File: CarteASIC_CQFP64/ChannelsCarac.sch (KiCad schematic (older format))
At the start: 29 parts, among them U1 ASIC_JUICE

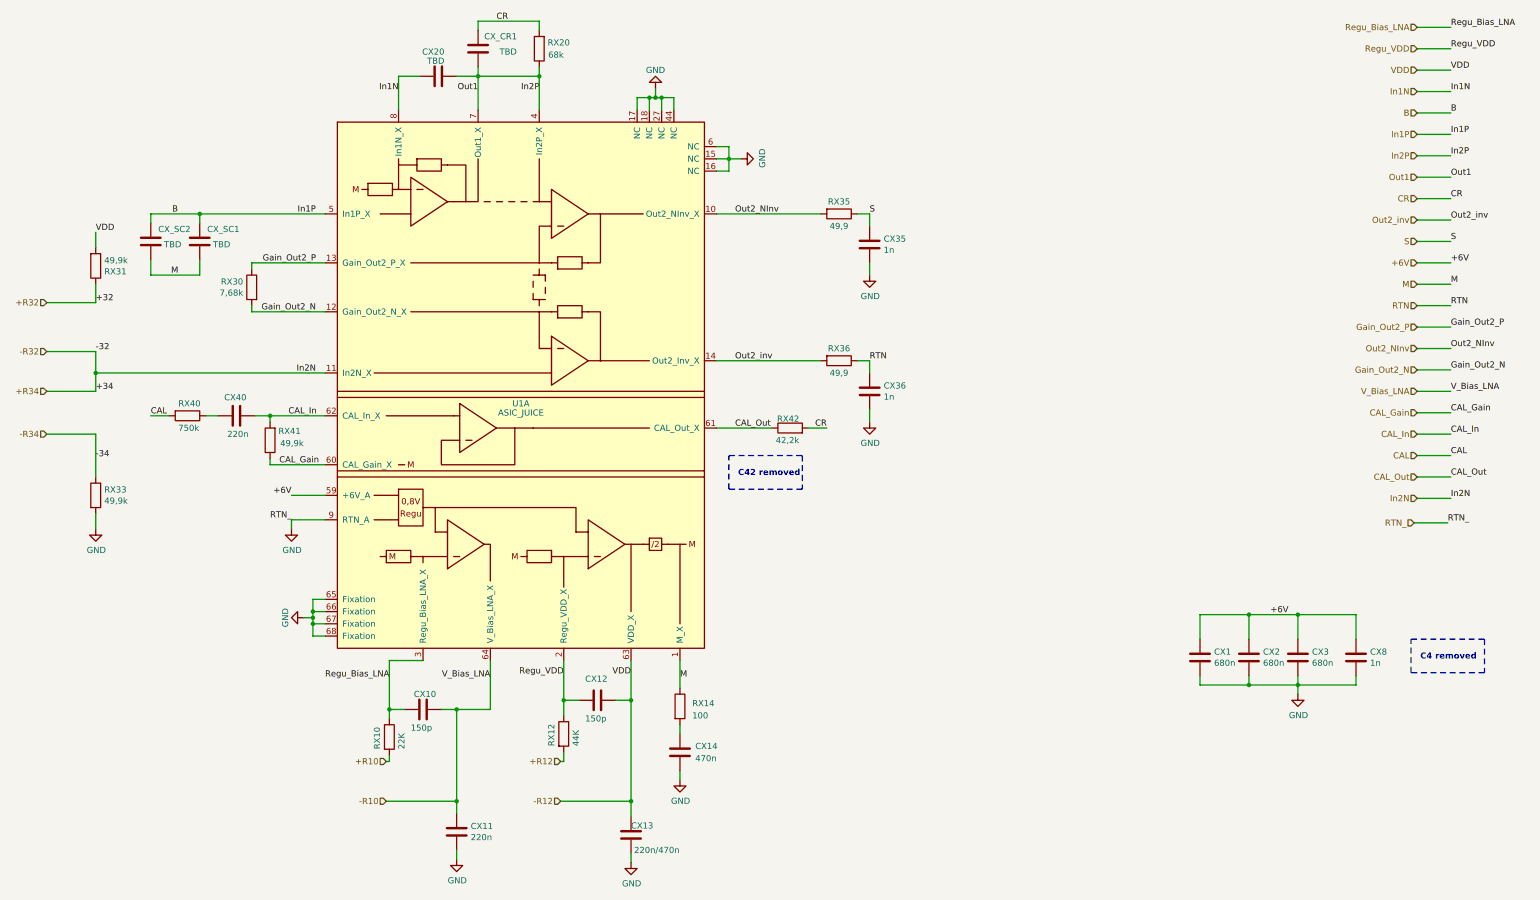
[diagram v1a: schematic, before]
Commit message: Mise en conformité valeurs PFM
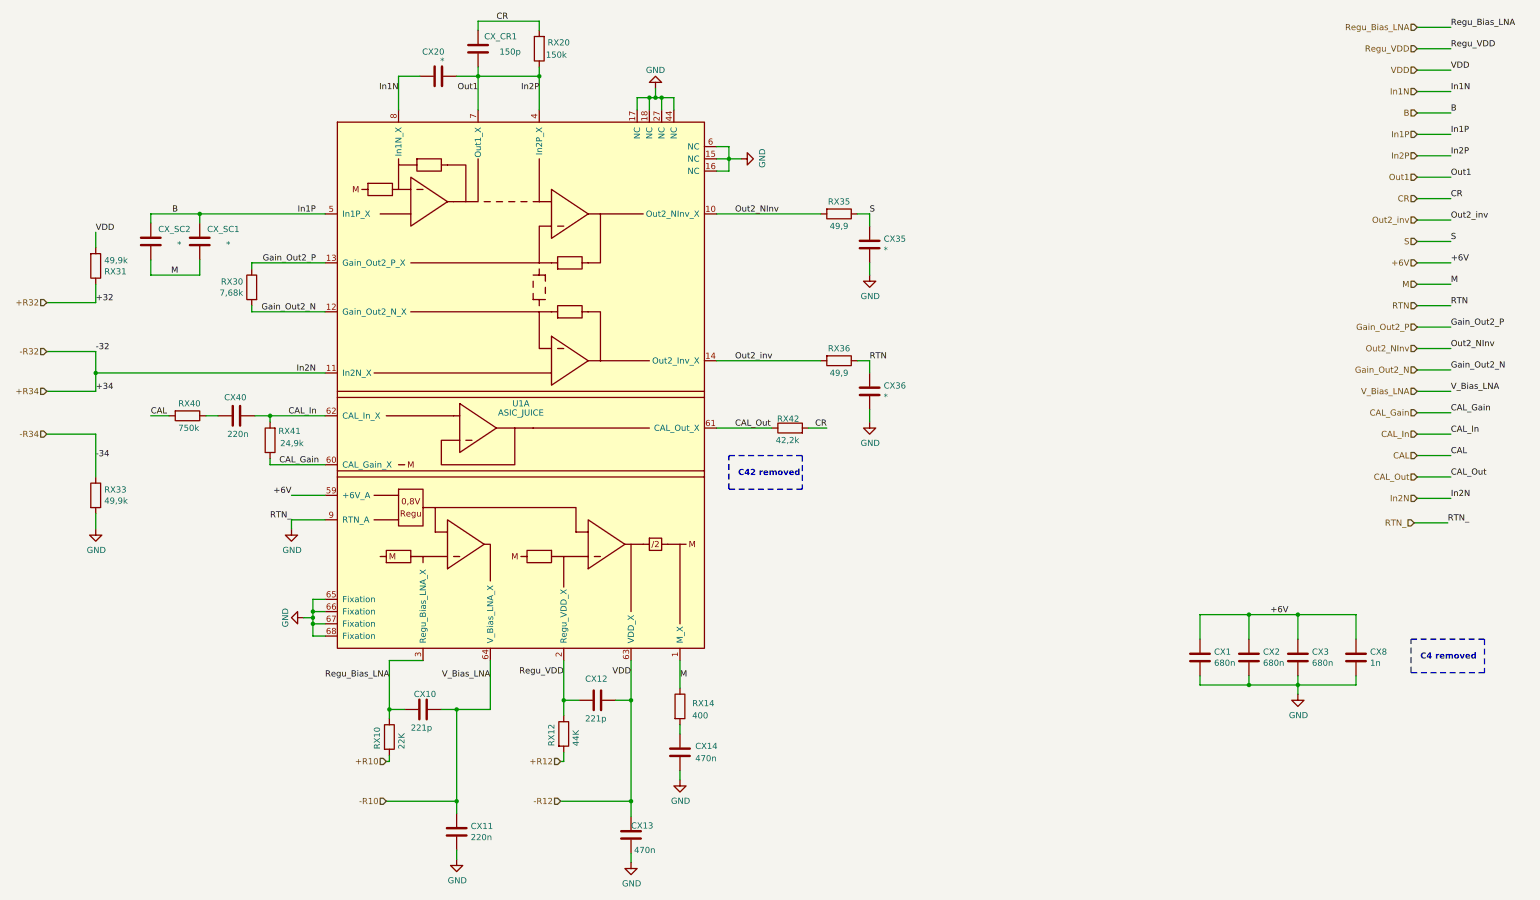
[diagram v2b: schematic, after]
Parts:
- CX10, CX12: value 150p -> 221p
- CX13: value 220n/470n -> 470n
- CX20, CX_SC1, CX_SC2: value TBD -> *
- CX35, CX36: value 1n -> *
- CX_CR1: value TBD -> 150p
- RX14: value 100 -> 400
- RX20: value 68k -> 150k
- RX41: value 49,9k -> 24,9k
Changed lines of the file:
@@
 AR Path="/5D9D35E7/5D83A418/5D7F2F74" Ref="CY12"  Part="1"
 F 0 "CX12" V 8075 7300 50  0000 L CNN
-F 1 "150p" V 8400 7300 50  0000 L CNN
+F 1 "221p" V 8400 7300 50  0000 L CNN
 F 2 "Capacitor_SMD:C_0603_1608Metric_Pad1.05x0.95mm_HandSolder" H 8288 7250 50  0001 C CNN
 F 3 "~" H 8250 7400 50  0001 C CNN
@@
 AR Path="/5D9D35E7/5D843251/5D8E789D" Ref="#PWR?"  Part="1"
 AR Path="/5D9D35E7/5D83A418/5D8E789D" Ref="#PWR?"  Part="1"
-F 0 "#PWR0117" H 8925 7800 50  0001 C CNN
+F 0 "#PWR0106" H 8925 7800 50  0001 C CNN
 F 1 "GND" H 8930 7877 50  0000 C CNN
 F 2 "" H 8925 8050 50  0001 C CNN
@@
 AR Path="/5D9D35E7/5D843251/5D8E7505" Ref="#PWR?"  Part="1"
 AR Path="/5D9D35E7/5D83A418/5D8E7505" Ref="#PWR?"  Part="1"
-F 0 "#PWR0118" H 8525 8475 50  0001 C CNN
+F 0 "#PWR0107" H 8525 8475 50  0001 C CNN
 F 1 "GND" H 8530 8552 50  0000 C CNN
 F 2 "" H 8525 8725 50  0001 C CNN
@@
 AR Path="/5D9D35E7/5D83A418/5D7F3986" Ref="CY35"  Part="1"
 F 0 "CX35" H 10590 3721 50  0000 L CNN
-F 1 "1n" H 10590 3630 50  0000 L CNN
+F 1 "*" H 10590 3630 50  0000 L CNN
 F 2 "Capacitor_SMD:C_0603_1608Metric_Pad1.05x0.95mm_HandSolder" H 10513 3525 50  0001 C CNN
 F 3 "~" H 10475 3675 50  0001 C CNN
@@
 AR Path="/5D9D35E7/5D83A418/5D7F398C" Ref="CY36"  Part="1"
 F 0 "CX36" H 10590 4921 50  0000 L CNN
-F 1 "1n" H 10590 4830 50  0000 L CNN
+F 1 "*" H 10590 4830 50  0000 L CNN
 F 2 "Capacitor_SMD:C_0603_1608Metric_Pad1.05x0.95mm_HandSolder" H 10513 4725 50  0001 C CNN
 F 3 "~" H 10475 4875 50  0001 C CNN
@@
 AR Path="/5D9D35E7/5D843251/5D96B6E7" Ref="#PWR?"  Part="1"
 AR Path="/5D9D35E7/5D83A418/5D96B6E7" Ref="#PWR?"  Part="1"
-F 0 "#PWR0119" H 10475 3675 50  0001 C CNN
+F 0 "#PWR0108" H 10475 3675 50  0001 C CNN
 F 1 "GND" H 10480 3752 50  0000 C CNN
 F 2 "" H 10475 3925 50  0001 C CNN
@@
 AR Path="/5D9D35E7/5D843251/5D96BF67" Ref="#PWR?"  Part="1"
 AR Path="/5D9D35E7/5D83A418/5D96BF67" Ref="#PWR?"  Part="1"
-F 0 "#PWR0120" H 10475 4875 50  0001 C CNN
+F 0 "#PWR0109" H 10475 4875 50  0001 C CNN
 F 1 "GND" H 10480 4952 50  0000 C CNN
 F 2 "" H 10475 5125 50  0001 C CNN
@@
 AR Path="/5D9D35E7/5D83A418/5D838645" Ref="RY20"  Part="1"
 F 0 "RX20" H 7525 2025 50  0000 L CNN
-F 1 "68k" H 7575 2125 50  0000 L CNN
+F 1 "150k" H 7550 2125 50  0000 L CNN
 F 2 "Resistor_SMD:R_0805_2012Metric_Pad1.15x1.40mm_HandSolder" V 7705 2075 50  0001 C CNN
 F 3 "~" H 7775 2075 50  0001 C CNN
@@
 AR Path="/5D9D35E7/5D843251/5D884FFA" Ref="#PWR?"  Part="1"
 AR Path="/5D9D35E7/5D83A418/5D884FFA" Ref="#PWR?"  Part="1"
-F 0 "#PWR0123" H 13975 7100 50  0001 C CNN
+F 0 "#PWR0112" H 13975 7100 50  0001 C CNN
 F 1 "GND" H 13980 7177 50  0000 C CNN
 F 2 "" H 13975 7350 50  0001 C CNN
@@
 AR Path="/5D9D35E7/5D843251/5E598485" Ref="#PWR?"  Part="1"
 AR Path="/5D9D35E7/5D83A418/5E598485" Ref="#PWR?"  Part="1"
-F 0 "#PWR0124" H 5850 6475 50  0001 C CNN
+F 0 "#PWR0113" H 5850 6475 50  0001 C CNN
 F 1 "GND" H 5850 6575 50  0000 C CNN
 F 2 "" H 5850 6725 50  0001 C CNN
@@
 AR Path="/5D9D35E7/5D843251/5E59CF62" Ref="#PWR?"  Part="1"
 AR Path="/5D9D35E7/5D83A418/5E59CF62" Ref="#PWR?"  Part="1"
-F 0 "#PWR0125" H 5750 5750 50  0001 C CNN
+F 0 "#PWR0114" H 5750 5750 50  0001 C CNN
 F 1 "GND" H 5755 5827 50  0000 C CNN
 F 2 "" H 5750 6000 50  0001 C CNN
@@
 AR Path="/5D9D35E7/5D843251/5E5A15CF" Ref="#PWR?"  Part="1"
 AR Path="/5D9D35E7/5D83A418/5E5A15CF" Ref="#PWR?"  Part="1"
-F 0 "#PWR0126" H 9425 2725 50  0001 C CNN
+F 0 "#PWR0115" H 9425 2725 50  0001 C CNN
 F 1 "GND" H 9430 2802 50  0000 C CNN
 F 2 "" H 9425 2975 50  0001 C CNN
@@
 AR Path="/5D9D35E7/5D843251/5E7A4666" Ref="#PWR?"  Part="1"
 AR Path="/5D9D35E7/5D83A418/5E7A4666" Ref="#PWR?"  Part="1"
-F 0 "#PWR0127" H 8725 2150 50  0001 C CNN
+F 0 "#PWR0116" H 8725 2150 50  0001 C CNN
 F 1 "GND" H 8725 2250 50  0000 C CNN
 F 2 "" H 8725 2400 50  0001 C CNN
@@
 AR Path="/5D9D35E7/5D83A418/5D917477" Ref="CY20"  Part="1"
 F 0 "CX20" V 7150 2250 50  0000 L CNN
-F 1 "TBD" V 7075 2250 50  0000 L CNN
+F 1 "*" V 7075 2250 50  0000 L CNN
 F 2 "Capacitor_SMD:C_0603_1608Metric_Pad1.05x0.95mm_HandSolder" H 6988 2150 50  0001 C CNN
 F 3 "~" H 6950 2300 50  0001 C CNN
@@
 AR Path="/5D9D35E7/5D83A418/5D92ED61" Ref="CY_CR"  Part="1"
 F 0 "CX_CR1" H 7325 2175 50  0000 L CNN
-F 1 "TBD" H 7450 2050 50  0000 L CNN
+F 1 "150p" H 7450 2050 50  0000 L CNN
 F 2 "Capacitor_SMD:C_0603_1608Metric_Pad1.05x0.95mm_HandSolder" H 7313 1925 50  0001 C CNN
 F 3 "~" H 7275 2075 50  0001 C CNN
@@
 AR Path="/5D9D35E7/5D83A418/5D987FFC" Ref="CY_SC1"  Part="1"
 F 0 "CX_SC1" H 4675 3750 50  0000 L CNN
-F 1 "TBD" H 4750 3625 50  0000 L CNN
+F 1 "*" H 4750 3625 50  0000 L CNN
 F 2 "Capacitor_SMD:C_0603_1608Metric_Pad1.05x0.95mm_HandSolder" H 5038 3500 50  0001 C CNN
 F 3 "~" H 5000 3650 50  0001 C CNN
@@
 AR Path="/5D9D35E7/5D83A418/5D9886E7" Ref="CY_SC2"  Part="1"
 F 0 "CX_SC2" H 4275 3750 50  0000 L CNN
-F 1 "TBD" H 4350 3625 50  0000 L CNN
+F 1 "*" H 4350 3625 50  0000 L CNN
 F 2 "Capacitor_SMD:C_0603_1608Metric_Pad1.05x0.95mm_HandSolder" H 4638 3500 50  0001 C CNN
 F 3 "~" H 4600 3650 50  0001 C CNN
@@
 AR Path="/5D9D35E7/5D843251/5D8A9AA9" Ref="#PWR?"  Part="1"
 AR Path="/5D9D35E7/5D83A418/5D8A9AA9" Ref="#PWR?"  Part="1"
-F 0 "#PWR0121" H 7100 8450 50  0001 C CNN
+F 0 "#PWR0110" H 7100 8450 50  0001 C CNN
 F 1 "GND" H 7105 8527 50  0000 C CNN
 F 2 "" H 7100 8700 50  0001 C CNN
@@
 AR Path="/5D9D35E7/5D83A418/5D7F2F7A" Ref="CY13"  Part="1"
 F 0 "CX13" H 8525 8575 50  0000 L CNN
-F 1 "220n/470n" H 8550 8375 50  0000 L CNN
+F 1 "470n" H 8550 8375 50  0000 L CNN
 F 2 "Capacitor_SMD:C_1210_3225Metric_Pad1.42x2.65mm_HandSolder" H 8563 8350 50  0001 C CNN
 F 3 "~" H 8525 8500 50  0001 C CNN
@@
 AR Path="/5D9D35E7/5D83A418/5D833442" Ref="RY14"  Part="1"
 F 0 "RX14" H 9025 7475 50  0000 L CNN
-F 1 "100" H 9025 7375 50  0000 L CNN
+F 1 "400" H 9025 7375 50  0000 L CNN
 F 2 "Resistor_SMD:R_0603_1608Metric_Pad1.05x0.95mm_HandSolder" V 8855 7450 50  0001 C CNN
 F 3 "~" H 8925 7450 50  0001 C CNN
@@
 AR Path="/5D9D35E7/5D83A418/5D837E24" Ref="RY41"  Part="1"
 F 0 "RX41" H 5325 5200 50  0000 L CNN
-F 1 "49,9k" H 5300 5300 50  0000 L CNN
+F 1 "24,9k" H 5300 5300 50  0000 L CNN
 F 2 "Resistor_SMD:R_0603_1608Metric_Pad1.05x0.95mm_HandSolder" V 5505 5275 50  0001 C CNN
 F 3 "~" H 5575 5275 50  0001 C CNN
@@
 AR Path="/5D9D35E7/5D83A418/5D7F19F6" Ref="CY10"  Part="1"
 F 0 "CX10" V 6700 7400 50  0000 L CNN
-F 1 "150p" V 6975 7375 50  0000 L CNN
+F 1 "221p" V 6975 7375 50  0000 L CNN
 F 2 "Capacitor_SMD:C_0603_1608Metric_Pad1.05x0.95mm_HandSolder" H 6863 7325 50  0001 C CNN
 F 3 "~" H 6825 7475 50  0001 C CNN
@@
 AR Path="/5D9D35E7/5D843251/5D9A4114" Ref="#PWR?"  Part="1"
 AR Path="/5D9D35E7/5D83A418/5D9A4114" Ref="#PWR?"  Part="1"
-F 0 "#PWR0122" H 4150 5750 50  0001 C CNN
+F 0 "#PWR0111" H 4150 5750 50  0001 C CNN
 F 1 "GND" H 4155 5827 50  0000 C CNN
 F 2 "" H 4150 6000 50  0001 C CNN
